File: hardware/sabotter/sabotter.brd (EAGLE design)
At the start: 92.5 x 80 mm, 112 parts, among them IC1 MAX3232CSE, IC2 MAX3232CSE, IC3 OKI-78SR-3.3/1.5-W36H-C, IC4 OKI-78SR-5/1.5-W36H-C, IC6 ATXMEGA256A3U-AU, IC7 LM4871M, T1 2n2222, T2 2n2222, T3 2n2222

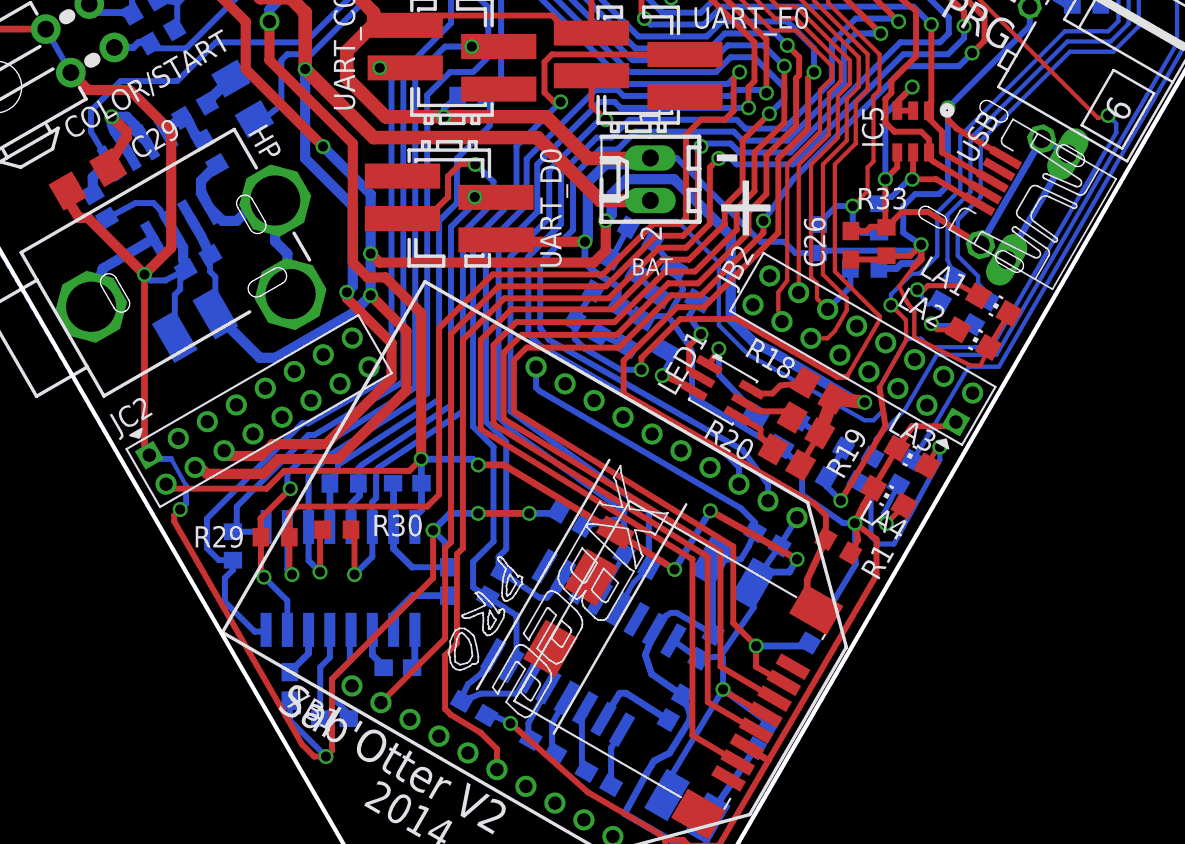
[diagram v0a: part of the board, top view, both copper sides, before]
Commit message: milling deleted on some connectors
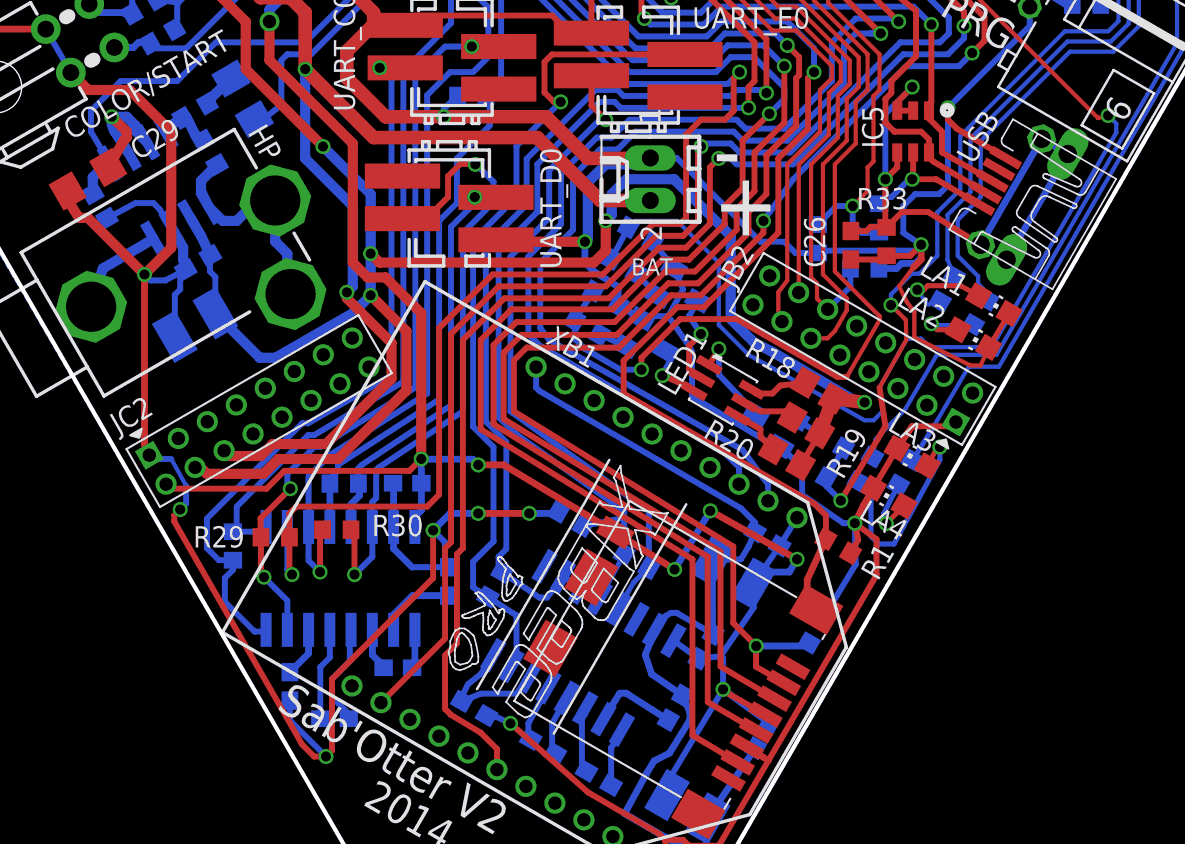
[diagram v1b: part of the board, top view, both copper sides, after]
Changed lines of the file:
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@@
 <layer number="21" name="tPlace" color="7" fill="1" visible="yes" active="yes"/>
 <layer number="22" name="bPlace" color="7" fill="1" visible="yes" active="yes"/>
-<layer number="23" name="tOrigins" color="15" fill="1" visible="no" active="yes"/>
-<layer number="24" name="bOrigins" color="15" fill="1" visible="no" active="yes"/>
+<layer number="23" name="tOrigins" color="15" fill="1" visible="yes" active="yes"/>
+<layer number="24" name="bOrigins" color="15" fill="1" visible="yes" active="yes"/>
 <layer number="25" name="tNames" color="7" fill="1" visible="yes" active="yes"/>
 <layer number="26" name="bNames" color="7" fill="1" visible="yes" active="yes"/>
@@
 <attribute name="MF" value="" x="48.273" y="24.891" size="1.778" layer="27" rot="R240" display="off"/>
 <attribute name="OC_FARNELL" value="1337916" x="48.273" y="24.891" size="1.778" layer="27" rot="R240" display="off"/>
-<attribute name="NAME" x="34.38326875" y="18.190828125" size="1.27" layer="25" rot="R150"/>
+<attribute name="NAME" x="49.85186875" y="39.882428125" size="1.27" layer="25" rot="R150"/>
 <attribute name="VALUE" x="37.273709375" y="44.43966875" size="1.27" layer="27" rot="R240"/>
 </element>
@@
 <element name="Q1" library="robotter_ic" package="HC49UP" value="" x="71.64" y="71.7058" smashed="yes" rot="R270">
 <attribute name="NAME" x="72.998" y="77.6344" size="1.27" layer="25" ratio="10"/>
-<attribute name="VALUE" x="67.449" y="77.4208" size="1.27" layer="27" ratio="10" rot="R270"/>
+<attribute name="VALUE" value="16 MHz" x="67.449" y="77.4208" size="1.27" layer="27" ratio="10" rot="R270"/>
 <attribute name="RS" value=" 547-6531" x="71.64" y="71.7058" size="1.778" layer="27" rot="R270" display="off"/>
 </element>
@@
 <wire x1="69.9516" y1="41.148" x2="69.596" y2="41.5036" width="0.3048" layer="1"/>
 <wire x1="69.596" y1="41.5036" x2="69.4944" y2="41.4528" width="0.254" layer="16"/>
-<wire x1="69.4944" y1="41.4528" x2="70.7136" y2="41.4528" width="0" layer="19" extent="1-16"/>
 <wire x1="72.1036" y1="41.451078125" x2="72.1868" y2="41.451078125" width="0.254" layer="16"/>
 <wire x1="72.1868" y1="41.451078125" x2="72.1868" y2="41.4274" width="0.254" layer="16"/>

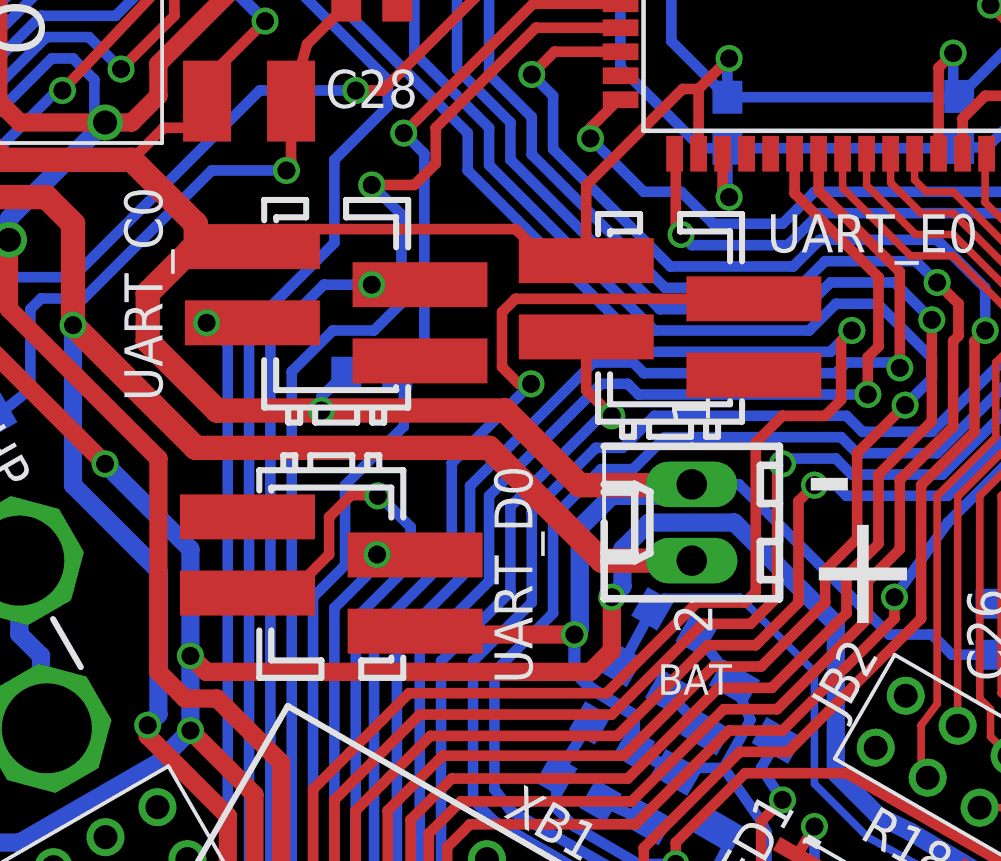
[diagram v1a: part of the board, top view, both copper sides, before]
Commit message: mouser component ref added
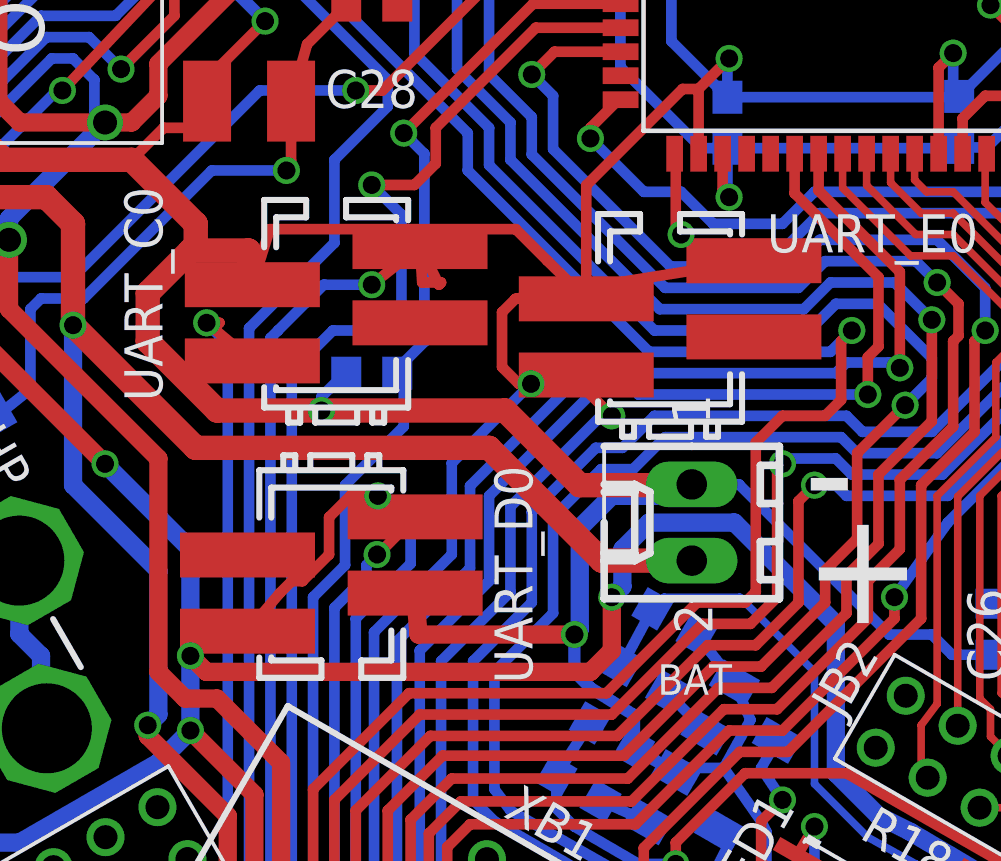
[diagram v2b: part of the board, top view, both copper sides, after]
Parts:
- BAT: device con-molex:6410-02 -> robotter_connector:6410-02
- T1, T2, T3: device transistor-neu-to92:SOT23-BEC -> robotter_ic:SOT23-BEC
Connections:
- net GND: now also UART_C0.2, UART_D0.2, UART_E0.2; no longer UART_C0.1, UART_D0.1, UART_E0.1
- net RX_C0_232: now also UART_C0.4; no longer UART_C0.3
- net RX_D0_232: now also UART_D0.4; no longer UART_D0.3
- net RX_E0_232: now also UART_E0.4; no longer UART_E0.3
- net TX_C0_232: now also UART_C0.1; no longer UART_C0.2
- net TX_D0_232: now also UART_D0.1; no longer UART_D0.2
- net TX_E0_232: now also UART_E0.1; no longer UART_E0.2
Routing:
- net GND: track 592.6 -> 597.7 mm
- net TX_C0_232: track 46.0 -> 48.3 mm
- net RX_E0_232: track 39.7 -> 38.4 mm
- net TX_D0_232: track 38.3 -> 38.9 mm
- net RX_D0_232: track 24.8 -> 25.3 mm
